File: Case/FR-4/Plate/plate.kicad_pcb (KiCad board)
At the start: 2 copper layers, 152.3 x 104.7 mm, 0 parts

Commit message: Some fix
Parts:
- added REF**: Hole_Cover_M2, Used_Footprints:Hole_Cover_M2, F.Cu at (92.5, 99.1)
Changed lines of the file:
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@@
     (tracks 0)
     (zones 0)
-    (modules 0)
+    (modules 1)
     (nets 1)
   )
@@
     (solder_mask_min_width 0.25)
     (aux_axis_origin 0 0)
-    (visible_elements FFFFFF7F)
+    (visible_elements 7FFFFFFF)
     (pcbplotparams
-      (layerselection 0x010fc_ffffffff)
-      (usegerberextensions false)
+      (layerselection 0x010f0_ffffffff)
+      (usegerberextensions true)
       (usegerberattributes false)
       (usegerberadvancedattributes false)
@@
       (plotinvisibletext false)
       (padsonsilk false)
-      (subtractmaskfromsilk false)
+      (subtractmaskfromsilk true)
       (outputformat 1)
       (mirror false)
-      (drillshape 1)
+      (drillshape 0)
       (scaleselection 1)
-      (outputdirectory ""))
+      (outputdirectory "Gerbers/"))
   )
   (net 0 "")
@@
     (uvia_dia 0.3)
     (uvia_drill 0.1)
+  )
+  (module Used_Footprints:Hole_Cover_M2 (layer F.Cu)
+    (at 92.48 99.12)
+    (fp_text reference REF** (at 0.09 -2.71) (layer F.SilkS)
+      (effects (font (size 1 1) (thickness 0.15)))
+    )
+    (fp_text value Hole_Cover_M2 (at 0.09 -3.71) (layer F.Fab)
+      (effects (font (size 1 1) (thickness 0.15)))
+    )
+    (pad 1 thru_hole circle (at 0 0) (size 4 4) (drill 2.2) (layers *.Cu *.Mask))
   )
   (gr_line (start 223.64 150.4325) (end 223.64 132.43) (layer Edge.Cuts) (width 0.05))
@@
     (polygon
       (pts
-        (xy 71.18 94.27) (xy 71.18 113.37) (xy 90.18 113.37) (xy 90.18 137.17) (xy 109.38 137.17)
-        (xy 109.38 134.77) (xy 128.38 134.77) (xy 128.38 127.67) (xy 147.48 127.67) (xy 147.48 122.97)
-        (xy 166.38 122.97) (xy 166.38 146.77) (xy 185.48 146.77) (xy 185.48 148.97) (xy 204.48 148.97)
+        (xy 71.18 94.27) (xy 71.18 113.37) (xy 90.18 113.37) (xy 90.18 137.2) (xy 109.38 137.2)
+        (xy 109.38 134.77) (xy 128.5 134.77) (xy 128.5 127.67) (xy 147.48 127.67) (xy 147.48 122.97)
+        (xy 166.38 122.97) (xy 166.38 146.77) (xy 185.48 146.77) (xy 185.48 149) (xy 204.48 149)
         (xy 204.48 151.47) (xy 223.68 151.47) (xy 223.68 132.37) (xy 205.01 132.37) (xy 204.68 53.67)
         (xy 185.58 53.67) (xy 185.58 51.37) (xy 166.57 51.37) (xy 166.57 46.57) (xy 147.38 46.57)
-        (xy 147.38 51.47) (xy 128.28 51.47) (xy 128.28 58.37) (xy 109.28 58.37) (xy 109.28 60.87)
+        (xy 147.38 51.4) (xy 128.28 51.4) (xy 128.28 58.37) (xy 109.28 58.37) (xy 109.28 60.87)
         (xy 90.18 60.87) (xy 90.18 94.27)
       )
@@
     (polygon
       (pts
-        (xy 71.18 94.27) (xy 71.18 113.37) (xy 90.18 113.37) (xy 90.18 137.17) (xy 109.38 137.17)
-        (xy 109.38 134.77) (xy 128.38 134.77) (xy 128.38 127.67) (xy 147.48 127.67) (xy 147.48 122.97)
-        (xy 166.38 122.97) (xy 166.38 146.77) (xy 185.48 146.77) (xy 185.48 148.97) (xy 204.48 148.97)
+        (xy 71.18 94.27) (xy 71.18 113.37) (xy 90.18 113.37) (xy 90.18 137.2) (xy 109.38 137.2)
+        (xy 109.38 134.77) (xy 128.5 134.77) (xy 128.5 127.67) (xy 147.48 127.67) (xy 147.48 122.97)
+        (xy 166.38 122.97) (xy 166.38 146.77) (xy 185.48 146.77) (xy 185.48 149) (xy 204.48 149)
         (xy 204.48 151.47) (xy 223.68 151.47) (xy 223.68 132.37) (xy 205.01 132.37) (xy 204.68 53.67)
         (xy 185.58 53.67) (xy 185.58 51.37) (xy 166.57 51.37) (xy 166.57 46.57) (xy 147.38 46.57)
-        (xy 147.38 51.47) (xy 128.28 51.47) (xy 128.28 58.37) (xy 109.28 58.37) (xy 109.28 60.87)
+        (xy 147.38 51.4) (xy 128.28 51.4) (xy 128.28 58.37) (xy 109.28 58.37) (xy 109.28 60.87)
         (xy 90.18 60.87) (xy 90.18 94.27)
       )

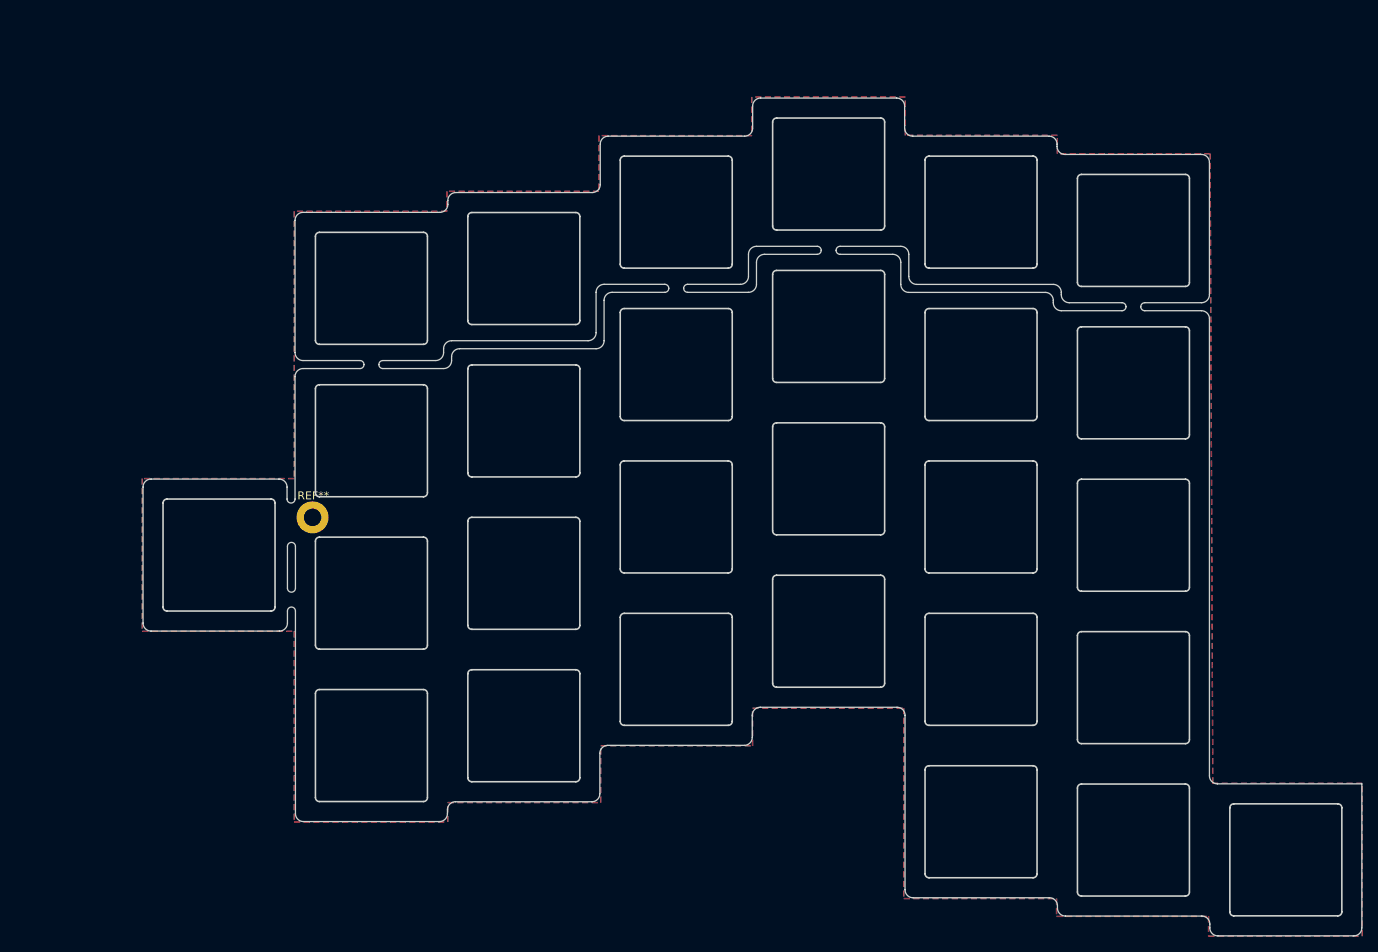
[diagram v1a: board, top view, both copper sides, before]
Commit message: Add new footprint for cutouts
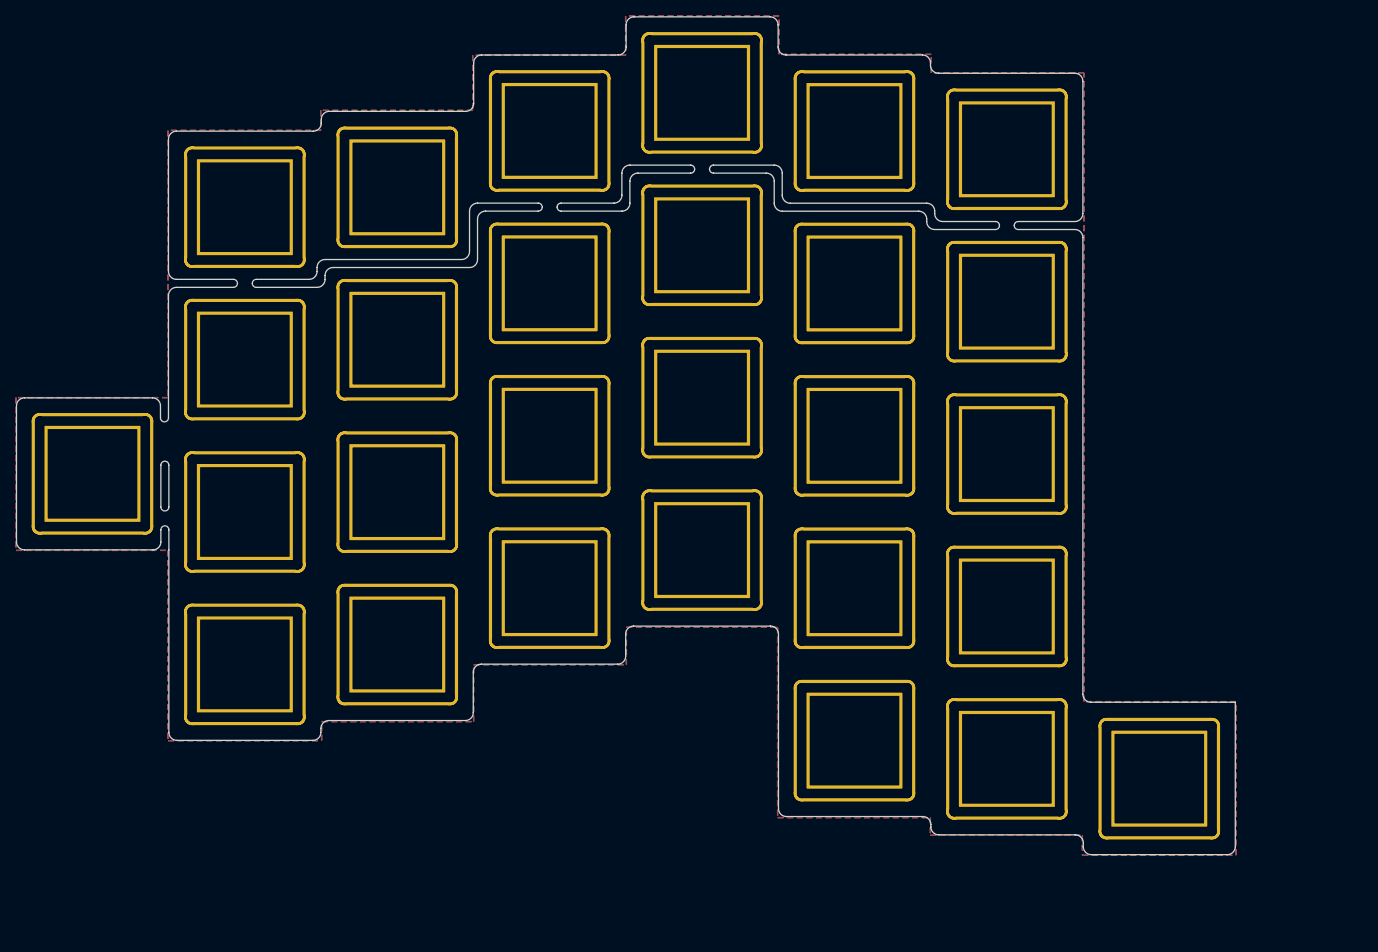
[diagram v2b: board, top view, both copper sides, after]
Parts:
- removed REF**: Hole_Cover_M2, Used_Footprints:Hole_Cover_M2
- added SW1: SW_Push, Used_Footprints:Cutout, F.Cu at (84.0, 60.4)
- added SW10: SW_Push, Used_Footprints:Cutout, F.Cu at (141.2, 65.1)
- added SW11: SW_Push, Used_Footprints:Cutout, F.Cu at (160.2, 69.9)
- added SW12: SW_Push, Used_Footprints:Cutout, F.Cu at (179.3, 72.2)
- added SW13: SW_Push, Used_Footprints:Cutout, F.Cu at (84.0, 98.5)
- added SW14: SW_Push, Used_Footprints:Cutout, F.Cu at (103.1, 96.0)
- added SW15: SW_Push, Used_Footprints:Cutout, F.Cu at (122.1, 88.9)
- added SW16: SW_Push, Used_Footprints:Cutout, F.Cu at (141.2, 84.2)
- added SW17: SW_Push, Used_Footprints:Cutout, F.Cu at (160.2, 88.9)
- added SW18: SW_Push, Used_Footprints:Cutout, F.Cu at (179.3, 91.2)
- added SW19: SW_Push, Used_Footprints:Cutout, F.Cu at (84.0, 117.5)
- added SW2: SW2, Used_Footprints:Cutout, F.Cu at (103.1, 57.9)
- added SW20: SW_Push, Used_Footprints:Cutout, F.Cu at (103.1, 115.0)
- added SW21: SW_Push, Used_Footprints:Cutout, F.Cu at (122.1, 108.0)
- added SW22: SW_Push, Used_Footprints:Cutout, F.Cu at (141.2, 103.2)
- added SW23: SW_Push, Used_Footprints:Cutout, F.Cu at (160.2, 108.0)
- added SW24: SW_Push, Used_Footprints:Cutout, F.Cu at (179.3, 110.3)
- added SW25: SW_Push, Used_Footprints:Cutout, F.Cu at (65.0, 93.7)
- added SW26: SW_Push, Used_Footprints:Cutout, F.Cu at (160.2, 127.0)
- added SW27: SW_Push, Used_Footprints:Cutout, F.Cu at (179.3, 129.3)
- added SW28: SW_Push, Used_Footprints:Cutout, F.Cu at (198.3, 131.8)
- added SW3: SW_Push, Used_Footprints:Cutout, F.Cu at (122.1, 50.8)
- added SW4: SW_Push, Used_Footprints:Cutout, F.Cu at (141.2, 46.1)
- added SW5: SW_Push, Used_Footprints:Cutout, F.Cu at (160.2, 50.8)
- added SW6: SW_Push, Used_Footprints:Cutout, F.Cu at (179.3, 53.1)
- added SW7: SW_Push, Used_Footprints:Cutout, F.Cu at (84.0, 79.4)
- added SW8: SW_Push, Used_Footprints:Cutout, F.Cu at (103.1, 76.9)
- added SW9: SW_Push, Used_Footprints:Cutout, F.Cu at (122.1, 69.9)
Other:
- outline, holes or cut-outs redrawn
